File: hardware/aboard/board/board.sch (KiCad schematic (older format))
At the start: 19 parts, among them P1 Power, P2 Analog, P3 Digital, P4 Digital, P5 CONN_01X01, P6 CONN_01X01, P7 CONN_01X01, P8 CONN_01X01, U1 24LC512, U10 ST25DV04K, U11 ST25DV04K, U2 AT25SF081-SSHD-X, U3 24LC512, U4 AT25SF081-SSHD-X, U5 24LC512, U6 LTC3406ES5, U7 LTC3406ES5, U8 Si5351A, U9 ICE40UP5K-SG48ITR

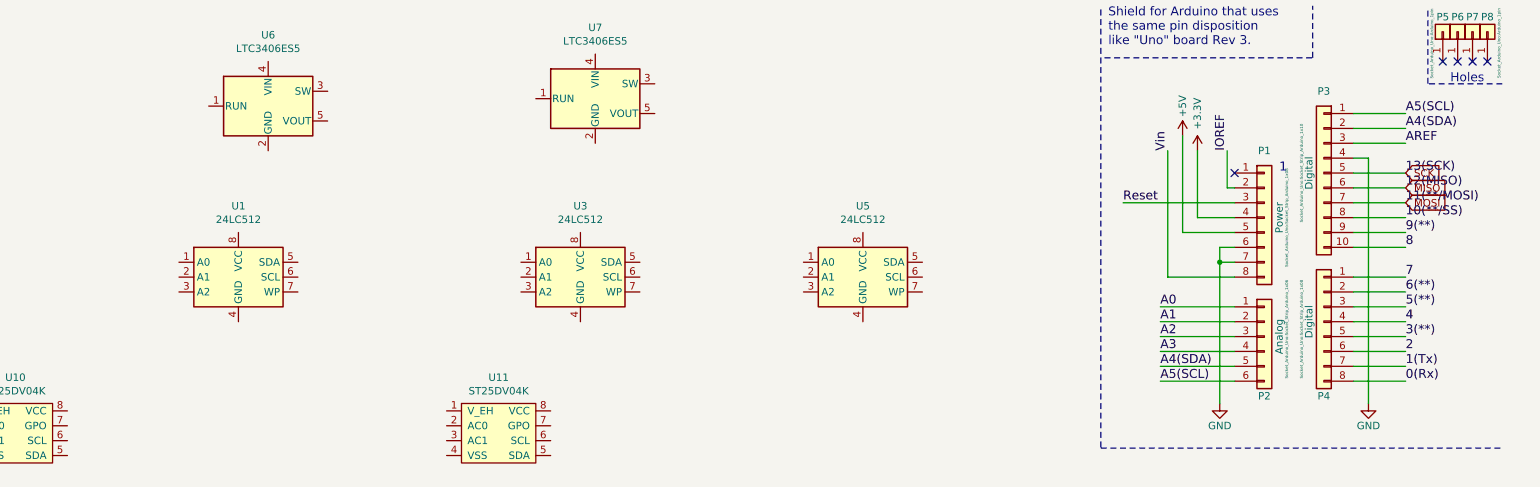
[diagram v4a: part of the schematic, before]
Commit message: board for OM13088UL: ST25DV04K symbol
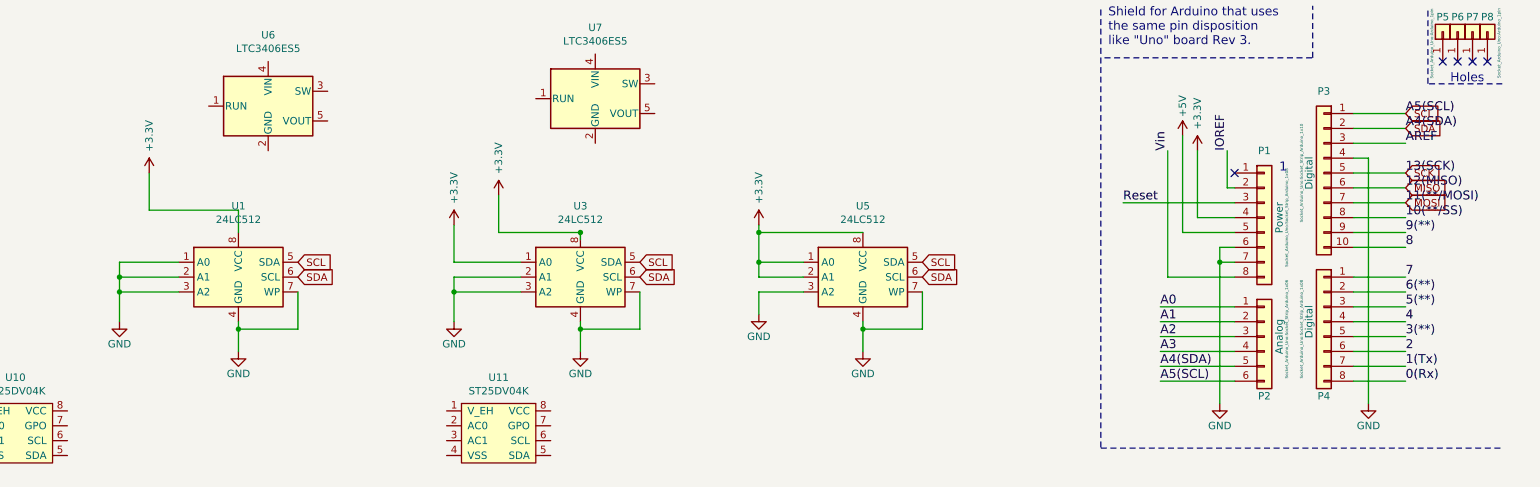
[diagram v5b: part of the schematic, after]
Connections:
- net A4(SDA) is gone; now on net SDA: P2.5 (Pin_5), P3.2 (Pin_2)
- net A5(SCL) is gone; now on net SCL: P2.6 (Pin_6), P3.1 (Pin_1)
- net +3V3: now also U1.8 (VCC), U3.1 (A0), U3.8 (VCC), U5.1 (A0), U5.2 (A1), U5.8 (VCC)
- net GND: now also U1.1 (A0), U1.2 (A1), U1.3 (A2), U1.4 (GND), U1.7 (WP), U3.2 (A1), U3.3 (A2), U3.4 (GND), U3.7 (WP), U5.3 (A2), U5.4 (GND), U5.7 (WP)
- net SCL: now reaches U3.5 (SDA)
- net SCL: now also U1.5 (SDA), U5.5 (SDA)
- net SDA: now reaches U3.6 (SCL)
- net SDA: now also U1.6 (SCL), U5.6 (SCL)
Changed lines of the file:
@@
 	1    0    0    -1
 $EndComp
+$Comp
+L power:GND #PWR05
+U 1 1 5D3A28E5
+P 1900 2600
+F 0 "#PWR05" H 1900 2350 50  0001 C CNN
+F 1 "GND" H 1900 2450 50  0000 C CNN
+F 2 "" H 1900 2600 50  0000 C CNN
+F 3 "" H 1900 2600 50  0000 C CNN
+	1    1900 2600
+	1    0    0    -1
+$EndComp
+Wire Wire Line
+	1900 2600 1900 2400
+Wire Wire Line
+	1900 2200 2300 2200
+Wire Wire Line
+	2300 2300 1900 2300
+Connection ~ 1900 2300
+Wire Wire Line
+	1900 2300 1900 2200
+Wire Wire Line
+	2300 2400 1900 2400
+Connection ~ 1900 2400
+Wire Wire Line
+	1900 2400 1900 2300
+$Comp
+L power:GND #PWR09
+U 1 1 5D3A539E
+P 4150 2600
+F 0 "#PWR09" H 4150 2350 50  0001 C CNN
+F 1 "GND" H 4150 2450 50  0000 C CNN
+F 2 "" H 4150 2600 50  0000 C CNN
+F 3 "" H 4150 2600 50  0000 C CNN
+	1    4150 2600
+	1    0    0    -1
+$EndComp
+$Comp
+L power:GND #PWR013
+U 1 1 5D3A5F2F
+P 6200 2550
+F 0 "#PWR013" H 6200 2300 50  0001 C CNN
+F 1 "GND" H 6200 2400 50  0000 C CNN
+F 2 "" H 6200 2550 50  0000 C CNN
+F 3 "" H 6200 2550 50  0000 C CNN
+	1    6200 2550
+	1    0    0    -1
+$EndComp
+Wire Wire Line
+	6500 2400 6200 2400
+Wire Wire Line
+	6200 2400 6200 2550
+Wire Wire Line
+	4600 2300 4150 2300
+Wire Wire Line
+	4150 2300 4150 2400
+Wire Wire Line
+	4600 2400 4150 2400
+Connection ~ 4150 2400
+Wire Wire Line
+	4150 2400 4150 2600
+$Comp
+L power:+3.3V #PWR012
+U 1 1 5D3A95AE
+P 6200 1950
+F 0 "#PWR012" H 6200 1800 50  0001 C CNN
+F 1 "+3.3V" V 6200 2200 50  0000 C CNN
+F 2 "" H 6200 1950 50  0000 C CNN
+F 3 "" H 6200 1950 50  0000 C CNN
+	1    6200 1950
+	1    0    0    -1
+$EndComp
+$Comp
+L power:+3.3V #PWR08
+U 1 1 5D3AA464
+P 4150 1950
+F 0 "#PWR08" H 4150 1800 50  0001 C CNN
+F 1 "+3.3V" V 4150 2200 50  0000 C CNN
+F 2 "" H 4150 1950 50  0000 C CNN
+F 3 "" H 4150 1950 50  0000 C CNN
+	1    4150 1950
+	1    0    0    -1
+$EndComp
+Wire Wire Line
+	4150 1950 4150 2200
+Wire Wire Line
+	4150 2200 4600 2200
+Wire Wire Line
+	6200 1950 6200 2000
+Wire Wire Line
+	6200 2300 6500 2300
+Wire Wire Line
+	6500 2200 6200 2200
+Connection ~ 6200 2200
+Wire Wire Line
+	6200 2200 6200 2300
+$Comp
+L power:GND #PWR07
+U 1 1 5D3AFF1D
+P 2700 2800
+F 0 "#PWR07" H 2700 2550 50  0001 C CNN
+F 1 "GND" H 2700 2650 50  0000 C CNN
+F 2 "" H 2700 2800 50  0000 C CNN
+F 3 "" H 2700 2800 50  0000 C CNN
+	1    2700 2800
+	1    0    0    -1
+$EndComp
+Wire Wire Line
+	2700 2800 2700 2650
+$Comp
+L power:GND #PWR011
+U 1 1 5D3B116F
+P 5000 2800
+F 0 "#PWR011" H 5000 2550 50  0001 C CNN
+F 1 "GND" H 5000 2650 50  0000 C CNN
+F 2 "" H 5000 2800 50  0000 C CNN
+F 3 "" H 5000 2800 50  0000 C CNN
+	1    5000 2800
+	1    0    0    -1
+$EndComp
+Wire Wire Line
+	5000 2800 5000 2650
+$Comp
+L power:GND #PWR014
+U 1 1 5D3B2412
+P 6900 2800
+F 0 "#PWR014" H 6900 2550 50  0001 C CNN
+F 1 "GND" H 6900 2650 50  0000 C CNN
+F 2 "" H 6900 2800 50  0000 C CNN
+F 3 "" H 6900 2800 50  0000 C CNN
+	1    6900 2800
+	1    0    0    -1
+$EndComp
+Wire Wire Line
+	6900 2800 6900 2650
+$Comp
+L power:+3.3V #PWR06
+U 1 1 5D3B3732
+P 2100 1600
+F 0 "#PWR06" H 2100 1450 50  0001 C CNN
+F 1 "+3.3V" V 2100 1850 50  0000 C CNN
+F 2 "" H 2100 1600 50  0000 C CNN
+F 3 "" H 2100 1600 50  0000 C CNN
+	1    2100 1600
+	1    0    0    -1
+$EndComp
+Wire Wire Line
+	2100 1600 2100 1850
+$Comp
+L power:+3.3V #PWR010
+U 1 1 5D3B4A89
+P 4450 1750
+F 0 "#PWR010" H 4450 1600 50  0001 C CNN
+F 1 "+3.3V" V 4450 2000 50  0000 C CNN
+F 2 "" H 4450 1750 50  0000 C CNN
+F 3 "" H 4450 1750 50  0000 C CNN
+	1    4450 1750
+	1    0    0    -1
+$EndComp
+Wire Wire Line
+	4450 1750 4450 2000
+Wire Wire Line
+	2100 1850 2700 1850
+Wire Wire Line
+	2700 1850 2700 2000
+Wire Wire Line
+	4450 2000 5000 2000
+Wire Wire Line
+	6200 2000 6900 2000
+Connection ~ 6200 2000
+Wire Wire Line
+	6200 2000 6200 2200
+Text GLabel 10550 1200 2    50   Input ~ 0
+SCL
+Text GLabel 10550 1300 2    50   Input ~ 0
+SDA
+Text GLabel 3100 2200 2    50   Input ~ 0
+SCL
+Text GLabel 3100 2300 2    50   Input ~ 0
+SDA
+Text GLabel 5400 2200 2    50   Input ~ 0
+SCL
+Text GLabel 5400 2300 2    50   Input ~ 0
+SDA
+Text GLabel 7300 2200 2    50   Input ~ 0
+SCL
+Text GLabel 7300 2300 2    50   Input ~ 0
+SDA
+Wire Wire Line
+	3100 2400 3100 2650
+Wire Wire Line
+	3100 2650 2700 2650
+Connection ~ 2700 2650
+Wire Wire Line
+	2700 2650 2700 2600
+Wire Wire Line
+	5400 2400 5400 2650
+Wire Wire Line
+	5400 2650 5000 2650
+Connection ~ 5000 2650
+Wire Wire Line
+	5000 2650 5000 2600
+Wire Wire Line
+	7300 2400 7300 2650
+Wire Wire Line
+	7300 2650 6900 2650
+Connection ~ 6900 2650
+Wire Wire Line
+	6900 2650 6900 2600
+Wire Wire Line
+	5000 2000 5000 2050
+Connection ~ 5000 2000
 $EndSCHEMATC

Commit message: board for OM13088UL: process 1
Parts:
- removed U11: ST25DV04K, symbol kilib:ST25DV04K
- removed U7: LTC3406ES5, Package_TO_SOT_SMD:TSOT-23-5, symbol Regulator_Switching:LTC3406ES5
- added C1, C2, C3, C4: C, symbol Device:C
- added L1: L, symbol Device:L
- added R1, R2: R, symbol Device:R
- added Y1: Crystal, symbol Device:Crystal
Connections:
- net 2 is gone; now on net COUNTER: P4.6 (Pin_6)
- net 3(**) is gone; now on net CSFPGA: P4.5 (Pin_5)
- net 4 is gone; now on net CSFLASH0: P4.4 (Pin_4)
- net 5(**) is gone; now on net CSFLASH1: P4.3 (Pin_3)
- net +3V3: now also U2.8 (VCC), U4.8 (VCC), U6.1 (RUN), U6.4 (VIN), U8.1 (VCC), U8.10 (IOVCC0), U9.1 (VCCIO_2), U9.22 (SPI_VCCIO1), U9.33 (VCCIO_0), C1.1, C3.2, C4.2
- net GND: now also U10.4 (VSS), U2.4 (GND), U4.4 (GND), U6.2 (GND), U8.8 (GND), U9.49 (GND), C1.2, C2.2, C3.1, C4.1, R2.2
- net MISO: now also U2.2 (SO/IO1), U9.14 (IOB_32a_SPI_SO)
- net MOSI: now also U2.5 (SI/IO0), U4.5 (SI/IO0), U9.17 (IOB_33b_SPI_SI)
- net SCK: now also U2.6 (SCK), U4.6 (SCK), U9.15 (IOB_34a_SPI_SCK)
- net SCL: now also U10.6 (SCL), U8.4 (SCL)
- net SDA: now also U10.5 (SDA), U8.5 (SDA)
- net CSFLASH0: now reaches U2.1 (~CS)
- net CSFLASH1: now reaches U4.1 (~CS)
- net at U6.3 (SW): now also L1.2
- net at U6.5 (VOUT): now also R1.2, R2.1
- net at U8.2 (XA): now also Y1.1
- net at U8.3 (XB): now also Y1.2
- net COUNTER: now reaches U8.6 (CLK2)
- net CSFPGA: now reaches U9.16 (IOB_35b_SPI_SS)
- new net 1V8: C2.1, L1.1, R1.1
- no-connect marks 5 -> 7
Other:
- moved on the sheet: U8
